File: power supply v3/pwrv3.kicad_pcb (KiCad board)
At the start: 2 copper layers, 38.3 x 37.5 mm, 47 parts, among them IC2 LM25145RGYR, IC3 LMR50410YQDBVRQ1, J1 1933189, J3 1933189, J4 Conn_01x04_Pin, Q1 CSD17577Q3A, Q2 CSD17577Q3A

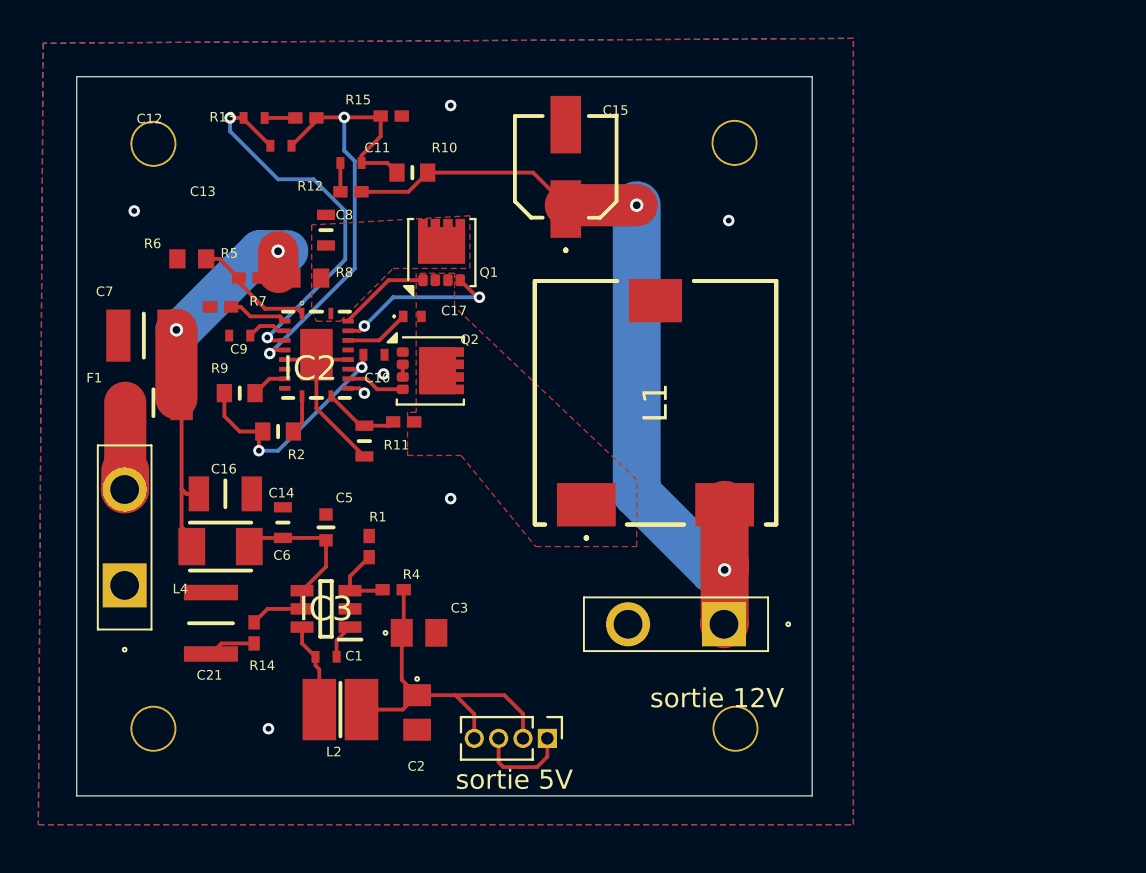
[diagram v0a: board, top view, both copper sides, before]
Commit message: new layout and pin moved
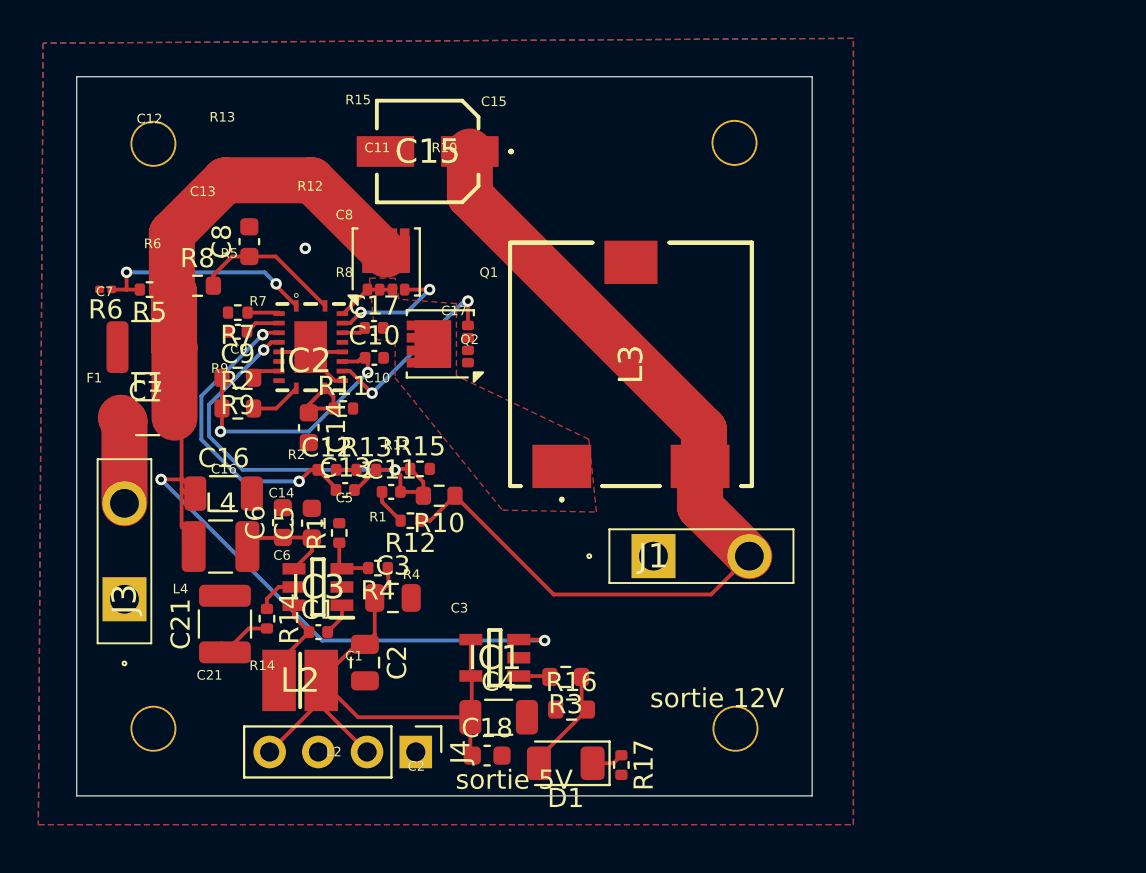
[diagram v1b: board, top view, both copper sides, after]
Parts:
- removed L1: SER1360-272KLD, 12V Power Board composants:SER1360272KLD
- added C18: 10uF, Capacitor_SMD:C_0603_1608Metric, F.Cu at (185.4, 109.4)
- added C4: 0.01uF, Capacitor_SMD:C_1206_3216Metric, F.Cu at (186.0, 107.4)
- added D1: LED, Diode_SMD:D_1206_3216Metric, F.Cu at (189.5, 109.8)
- added IC1: TLV3701IDBVR, footprint comparateur:SOT95P280X145-5N, F.Cu at (185.8, 104.3)
- added L3: 2.7uH 2.6mOhms, composant speciaux:SER1360272KLD, F.Cu at (192.9, 89.0)
- added R16: 250 ohms, Resistor_SMD:R_0603_1608Metric, F.Cu at (189.8, 107.0)
- added R17: 50 ohms, Resistor_SMD:R_0402_1005Metric, F.Cu at (192.4, 109.9)
- added R3: 250 ohms, Resistor_SMD:R_0603_1608Metric, F.Cu at (189.5, 105.3)
- C1: value GRM155R71C104KA88D -> 100nF; footprint 12V Power Board composants:CAPC1005X55N -> Capacitor_SMD:C_0402_1005Metric
- C10: value C1005X5R1V225K050BC -> 2.2uF; footprint 12V Power Board composants:CAPC1005X55N -> Capacitor_SMD:C_0402_1005Metric
- C11, C13: value CGA2B2X7R1H681K050BA -> 680pF; footprint 12V Power Board composants:CAPC1005X55N -> Capacitor_SMD:C_0402_1005Metric
- C12: value GRM155R71C822KA01D -> 8200pF; footprint 12V Power Board composants:CAPC1005X55N -> Capacitor_SMD:C_0402_1005Metric
- C14: value GRM1885C2A100JA01D -> 10pF 100Vdc; footprint 12V Power Board composants:CAPC1608X90N -> Capacitor_SMD:C_0603_1608Metric
- C15: value 20SVPF56MX -> 56uF 20 V; footprint 12V Power Board composants:16SVF82M -> composant speciaux:16SVF82M
- C16: value GRM31CR71H475KA12L -> 4.7UF; footprint 12V Power Board composants:CAPC3216X180N -> Capacitor_SMD:C_1206_3216Metric
- C17: footprint 12V Power Board composants:GCM155 -> Capacitor_SMD:C_0402_1005Metric
- C2: value C0805C106K8PACTU -> 10 uF 10 MOhms (2x); footprint 12V Power Board composants:C0805 -> Capacitor_SMD:C_0805_2012Metric
- C21: value C3225X7S2A475M200AB -> 4.7 uF; footprint 12V Power Board composants:CAPC3225X200N -> Capacitor_SMD:C_1210_3225Metric
- C3: footprint 12V Power Board composants:C0805 -> Capacitor_SMD:C_0805_2012Metric
- C5: value GRM188R72A104KA35J -> 0.1 uF; footprint 12V Power Board composants:GRM18x -> Capacitor_SMD:C_0603_1608Metric
- C6: value C1608X5R1E106M080AC -> 10uF; footprint 12V Power Board composants:CAPC1608X80N -> Capacitor_SMD:C_0603_1608Metric
- C7: value GRM32ER71H475KA88L -> 4.7uF 50V; footprint 12V Power Board composants:CAPC3225X270N -> Capacitor_SMD:C_1210_3225Metric
- C8: footprint 12V Power Board composants:CAPC1608X90N -> Capacitor_SMD:C_0603_1608Metric
- C9: value GRM155R71C563KA88D -> 56nF; footprint 12V Power Board composants:CAPC1005X55N -> Capacitor_SMD:C_0402_1005Metric
- F1: footprint 12V Power Board composants:FUSC3216X117N -> Fuse:Fuse_1206_3216Metric
- IC2: footprint 12V Power Board composants:RGY0020B -> composant speciaux:RGY0020B
- IC3: footprint converter:SOT95P280X145-6N -> composant speciaux:SOT95P280X145-6N
- J1: value 1933189 -> 1.5 mm; footprint 12V Power Board composants:1933189 -> composant speciaux:1933189
- J3: footprint 12V Power Board composants:1933189 -> composant speciaux:1933189
- J4: value Conn_01x04_Pin -> Conn_01x04_Pin 1.27mm; footprint Connector_PinHeader_1.27mm:PinHeader_1x04_P1.27mm_Vertical -> Connector_PinHeader_2.54mm:PinHeader_1x04_P2.54mm_Vertical
- L2: value 74438336047 -> 4.7uH; footprint 12V Power Board composants:INDC3030X200N -> composant speciaux:INDC3030X200N
- L4: value NLCV32T-R33M-EFRD -> 0.33uH 0.035ohm; footprint 12V Power Board composants:INDPM3225X240N -> Inductor_SMD:L_1210_3225Metric
- Q1: value CSD17577Q3A -> 35A, 30V
- Q2: value CSD17577Q3A -> 35A Id, 30V Vds
- R1: value CRCW040222K1FKED -> 22.1k; footprint 12V Power Board composants:RESC1005X40N -> Resistor_SMD:R_0402_1005Metric
- R10: value RC0603FR-0718KL -> 18k; footprint 12V Power Board composants:RESC1608X55N -> Resistor_SMD:R_0603_1608Metric
- R11: value CRCW04021K24FKED -> 1.24k; footprint 12V Power Board composants:RESC1005X40N -> Resistor_SMD:R_0402_1005Metric
- R12: value CRCW04022K49FKED -> 2.49k; footprint 12V Power Board composants:RESC1005X40N -> Resistor_SMD:R_0402_1005Metric
- R13: value CRCW04022K37FKED -> 2.37k; footprint 12V Power Board composants:RESC1005X40N -> Resistor_SMD:R_0402_1005Metric
- R14: value CRCW04021R00FKED -> 1/16watt 1ohms; footprint 12V Power Board composants:RESC1005X40N -> Resistor_SMD:R_0402_1005Metric
- R15: value CRCW04021K27FKED -> 1.27K; footprint 12V Power Board composants:RESC1005X40N -> Resistor_SMD:R_0402_1005Metric
- R2: value RC0603FR-0720KL -> 20k; footprint 12V Power Board composants:RESC1608X55N -> Resistor_SMD:R_0603_1608Metric
- R4: value CRCW040288K7FKED -> 88.7K; footprint 12V Power Board composants:RESC1005X40N -> Resistor_SMD:R_0402_1005Metric
- R5: value CRCW040269K8FKED -> 69.8k; footprint 12V Power Board composants:RESC1005X40N -> Resistor_SMD:R_0402_1005Metric
- R6: value CRCW06038K25FKEA -> 8.25k; footprint 12V Power Board composants:RESC1608X50N -> Resistor_SMD:R_0201_0603Metric
- R7: value CRCW040239K2FKED -> 39.2k; footprint 12V Power Board composants:RESC1005X40N -> Resistor_SMD:R_0402_1005Metric
- R8: value CRCW06032R10FKEA -> 2.1ohms 1%; footprint 12V Power Board composants:RESC1608X50N -> Resistor_SMD:R_0603_1608Metric
- R9: value RC0603FR-0720KL -> 20 kOhms; footprint 12V Power Board composants:RESC1608X55N -> Resistor_SMD:R_0603_1608Metric
- moved C12 18.7 mm to (177.1, 94.5)
- moved R13 18.6 mm to (179.1, 94.5)
- moved R15 18.5 mm to (181.9, 94.5)
- moved C13 18.3 mm to (178.0, 95.5)
- moved R12 17.4 mm to (181.4, 97.2)
- moved C11 17.3 mm to (180.4, 95.7)
- moved R10 16.9 mm to (182.9, 95.8)
- moved C15 7.24 mm to (182.3, 77.9), turned to 180 degrees
- moved J4 6.90 mm to (181.7, 109.2)
- moved R8 5.71 mm to (170.3, 84.9)
- moved R5 5.23 mm to (167.8, 85.1)
- moved J1 5.11 mm to (194.1, 99.0), turned to 0 degrees
- moved R6 4.76 mm to (165.5, 85.1)
- moved C8 4.04 mm to (173.0, 82.6)
- moved C2 3.76 mm to (179.0, 104.5)
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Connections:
- net Net-(J4-Pin_2) renamed +5V
- C16 pad 1: Net-(C16-Pad1) -> +12V
- C7 pad 1: Net-(C16-Pad1) -> +12V
- F1 pad 2: Net-(C16-Pad1) -> +12V
- J1 pad 1: Net-(C15-+) -> GND
- J1 pad 2: GND -> Net-(C15-+)
- L4 pad 1: Net-(C16-Pad1) -> +12V
- Q1 pad 5: Net-(IC2-VIN) -> +12V
- R5 pad 1: Net-(C16-Pad1) -> +12V
- R8 pad 1: Net-(C16-Pad1) -> +12V
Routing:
- net +12V: track 0.00 -> 60.5 mm, vias 0 -> 2
- net Net-(C16-Pad1): track 22.5 -> 0.00 mm, vias 2 -> 0
- net +5V: track 18.9 -> 31.9 mm
- net GND: track 16.5 -> 6.17 mm, vias 7 -> 1
- net Net-(IC2-VIN): track 0.00 -> 7.85 mm
- net Net-(IC2-LO): track 3.08 -> 10.3 mm, vias 0 -> 2
- net 2.5v: track 0.00 -> 5.67 mm
- net Net-(IC2-EN/UVLO): track 6.31 -> 11.9 mm, vias 0 -> 2
- net Net-(C15-+): track 43.4 -> 48.1 mm, vias 2 -> 0
- net Net-(IC2-COMP): track 20.4 -> 16.4 mm
- net Net-(IC3-EN): track 11.1 -> 7.64 mm
- net Net-(IC2-HO): track 8.95 -> 6.57 mm
- net Net-(IC2-SW): track 5.69 -> 3.38 mm
- net Net-(IC2-BST): track 3.39 -> 1.27 mm
- net Net-(D1-K): track 0.00 -> 1.67 mm
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- removed copper zone on F.Cu, net Net-(IC2-VIN)

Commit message: entree comparateur 5V
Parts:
- added H1: MountingHole, MountingHole:MountingHole_2.2mm_M2, F.Cu at (216.5, 106.5)
- added H4: MountingHole, MountingHole:MountingHole_2.2mm_M2, F.Cu at (216.5, 112.4)
- added R18: R, Resistor_SMD:R_0402_1005Metric, F.Cu at (189.1, 102.0)
- added R19: R, Resistor_SMD:R_0402_1005Metric, F.Cu at (187.1, 102.0)
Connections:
- IC1 pad 3: +12V -> Net-(IC1-IN+)
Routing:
- net Net-(IC1-IN+): track 0.00 -> 2.58 mm
- net +12V: track 60.5 -> 61.4 mm

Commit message: retracing
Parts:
- removed H1, H4: MountingHole, MountingHole:MountingHole_2.2mm_M2
- moved R6 6.89 mm to (172.2, 83.7), turned to -90 degrees
- moved R5 6.72 mm to (173.5, 81.5), turned to -90 degrees
- moved R8 5.92 mm to (175.2, 81.6), turned to -90 degrees
- moved R18 5.06 mm to (184.1, 101.3), turned to 0 degrees
- moved C15 4.95 mm to (187.2, 77.8)
- moved C8 4.12 mm to (176.9, 83.8)
- moved R17 3.51 mm to (195.0, 107.6), turned to 90 degrees
- moved D1 3.37 mm to (192.1, 107.6)
- moved R11 2.90 mm to (180.8, 91.8)
- moved R10 2.80 mm to (183.3, 98.6), turned to 90 degrees
- moved R15 2.58 mm to (183.8, 96.2)
- moved R16 2.23 mm to (191.4, 105.5), turned to 180 degrees
- moved F1 2.12 mm to (166.4, 90.1), turned to 90 degrees
- moved C11 2.02 mm to (182.0, 96.9), turned to 90 degrees
- moved C7 1.93 mm to (167.9, 86.2), turned to 0 degrees
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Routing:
- net +12V: track 61.4 -> 51.3 mm
- net Net-(IC2-EN/UVLO): track 11.9 -> 5.98 mm, vias 2 -> 0
- net Net-(C15-+): track 48.1 -> 44.1 mm
- net Net-(IC2-VIN): track 7.85 -> 4.27 mm
- net Net-(IC2-FB): track 24.7 -> 27.8 mm
- net +5V: track 31.9 -> 34.7 mm
- net Net-(IC2-ILIM): track 4.24 -> 6.86 mm
- net Net-(IC2-COMP): track 16.4 -> 18.8 mm
- net Net-(IC2-VCC): track 14.1 -> 11.7 mm
- net 2.5v: track 5.67 -> 3.84 mm
- net Net-(C21-Pad1): track 3.48 -> 1.79 mm
- net Net-(IC2-SW): track 3.38 -> 5.02 mm
- net Net-(IC2-SYNCIN): track 1.47 -> 2.91 mm
- net Net-(IC3-EN): track 7.64 -> 9.02 mm
- net Net-(C11-Pad1): track 1.90 -> 0.89 mm
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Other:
- board text added: "12V"
- board text added: "5V"
- board text added: "FUSE"
- board text added: "GND"
- board text removed: "C1"
- board text removed: "C10"
- board text removed: "C11"
- board text removed: "C12"
- board text removed: "C14"
- board text removed: "C15"
- board text removed: "C16"
- board text removed: "C17"
- board text removed: "C3"
- board text removed: "C5"
- board text removed: "C6"
- board text removed: "C9"
- board text removed: "F1"
- board text removed: "L2"
- board text removed: "L4"
- board text removed: "Q1"
- board text removed: "Q2"
- board text removed: "R1"
- board text removed: "R10"
- board text removed: "R11"
- board text removed: "R13"
- board text removed: "R14"
- board text removed: "R15"
- board text removed: "R2"
- board text removed: "R4"
- board text removed: "R5"
- board text removed: "R7"
- board text removed: "R8"
- board text removed: "R9"
- board text removed: "sortie 12V"
- board text removed: "sortie 5V"

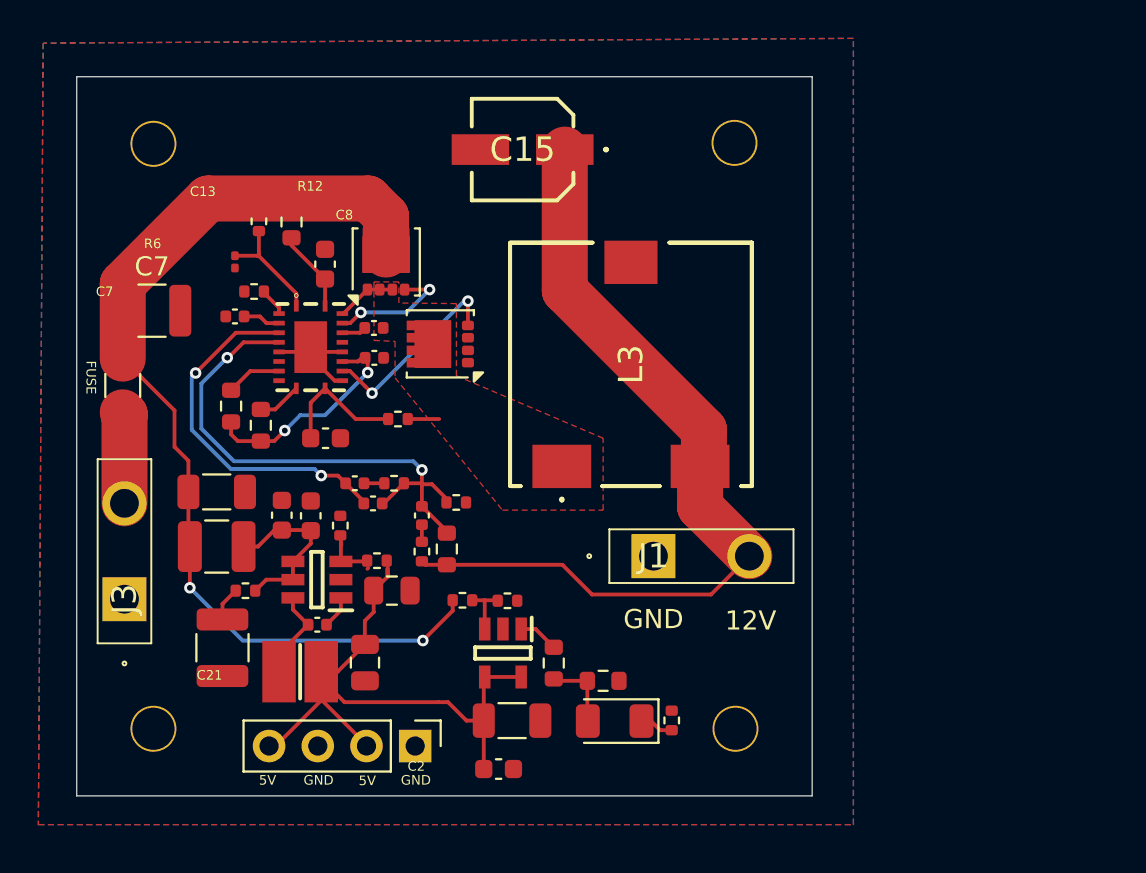
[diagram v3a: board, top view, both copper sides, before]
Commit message: flip Q2 transistor
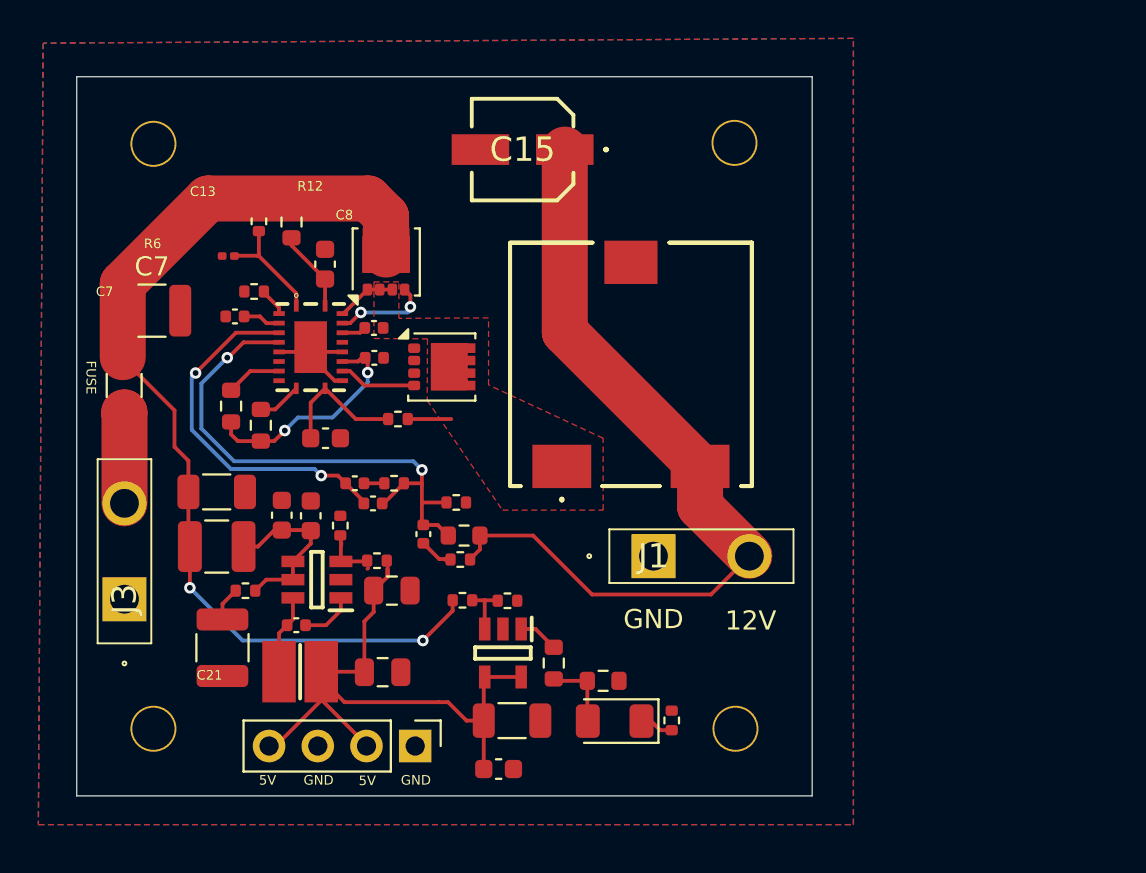
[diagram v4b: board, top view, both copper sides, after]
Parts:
- moved R12 2.04 mm to (184.0, 99.2), turned to 180 degrees
- moved Q2 1.19 mm to (183.0, 89.1), turned to 0 degrees
- moved R10 1.14 mm to (184.2, 97.9), turned to 180 degrees
- moved C1 1.10 mm to (175.4, 102.6)
- moved C2 1.05 mm to (179.9, 105.0), turned to 0 degrees
- moved C11 0.97 mm to (182.1, 97.8)
- moved R6 0.46 mm to (171.9, 83.3), turned to 180 degrees
- moved F1 0.07 mm to (166.5, 90.1)
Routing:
- net Net-(IC2-LO): track 10.3 -> 4.05 mm, vias 2 -> 0
- net Net-(IC2-HO): track 6.57 -> 5.01 mm
- net Net-(C15-+): track 44.1 -> 42.8 mm
- net Net-(IC3-CB): track 1.71 -> 2.82 mm
- net Net-(C11-Pad1): track 0.89 -> 1.77 mm
- net +5V: track 34.7 -> 35.5 mm
- net Net-(IC3-SW): track 4.82 -> 4.15 mm
- net Net-(IC2-SW): track 5.02 -> 5.65 mm
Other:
- board text removed: "C2"
